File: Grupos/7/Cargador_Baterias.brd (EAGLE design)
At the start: 70.3 x 59.3 mm, 48 parts, among them M1 NUCLEO-L452RE, U1 MCP73830T-2AAI/MYY, U2 MCP73830T-2AAI/MYY, U3 MCP73830T-2AAI/MYY

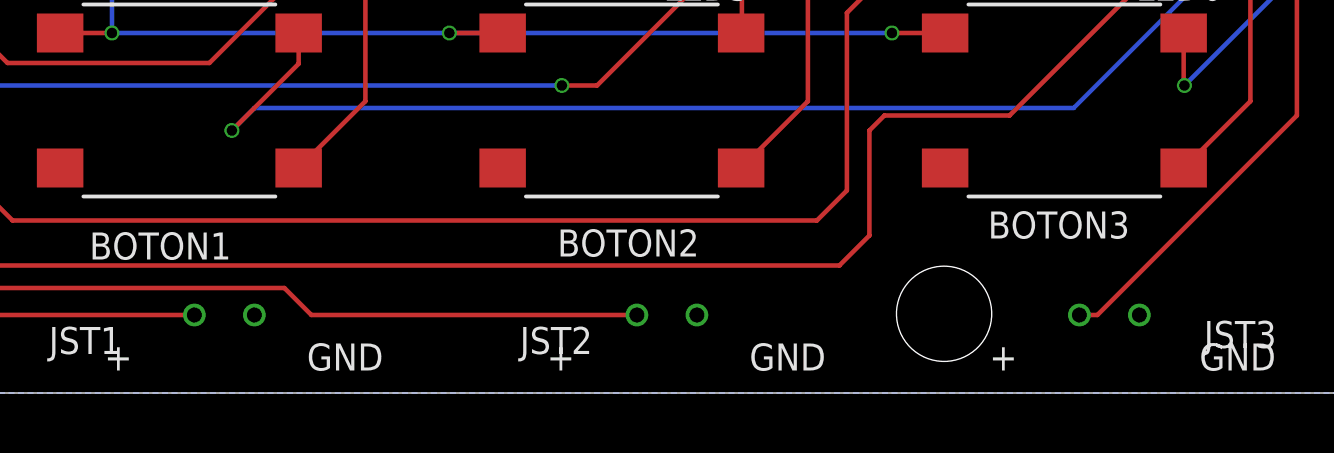
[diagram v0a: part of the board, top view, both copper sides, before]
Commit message: Se arregla JST
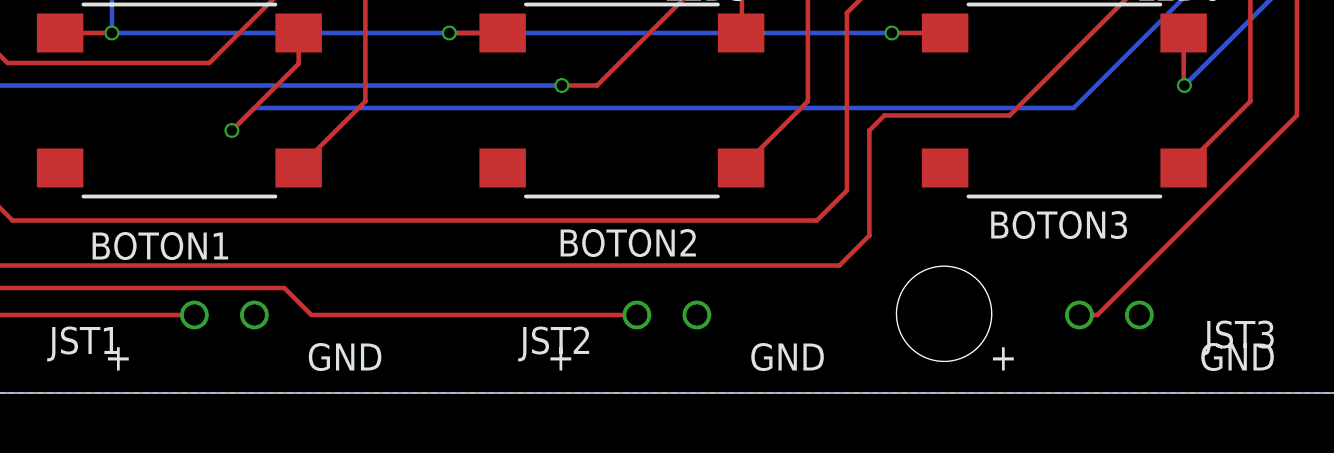
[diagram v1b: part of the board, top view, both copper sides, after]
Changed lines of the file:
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@@
 <drawing>
 <settings>
-<setting alwaysvectorfont="no"/>
+<setting alwaysvectorfont="yes"/>
 <setting verticaltext="up"/>
 </settings>
@@
 <layer number="1" name="Top" color="4" fill="1" visible="yes" active="yes"/>
 <layer number="16" name="Bottom" color="1" fill="1" visible="yes" active="yes"/>
-<layer number="17" name="Pads" color="2" fill="1" visible="no" active="yes"/>
-<layer number="18" name="Vias" color="2" fill="1" visible="no" active="yes"/>
+<layer number="17" name="Pads" color="2" fill="1" visible="yes" active="yes"/>
+<layer number="18" name="Vias" color="2" fill="1" visible="yes" active="yes"/>
 <layer number="19" name="Unrouted" color="6" fill="1" visible="no" active="yes"/>
 <layer number="20" name="Dimension" color="24" fill="1" visible="no" active="yes"/>
 <layer number="21" name="tPlace" color="7" fill="1" visible="no" active="yes"/>
 <layer number="22" name="bPlace" color="7" fill="1" visible="no" active="yes"/>
-<layer number="23" name="tOrigins" color="15" fill="1" visible="no" active="yes"/>
-<layer number="24" name="bOrigins" color="15" fill="1" visible="no" active="yes"/>
+<layer number="23" name="tOrigins" color="15" fill="1" visible="yes" active="yes"/>
+<layer number="24" name="bOrigins" color="15" fill="1" visible="yes" active="yes"/>
 <layer number="25" name="tNames" color="7" fill="1" visible="yes" active="yes"/>
 <layer number="26" name="bNames" color="7" fill="1" visible="no" active="yes"/>
@@
 <wire x1="31" y1="41.6" x2="31.0744" y2="41.5256" width="0.1524" layer="1"/>
 <wire x1="31.0744" y1="41.5256" x2="32.0256" y2="41.5256" width="0.1524" layer="1"/>
+<wire x1="59.23" y1="42.264" x2="64.31" y2="40.71500625" width="0" layer="19" extent="1-1"/>
+<wire x1="51.05" y1="39.75" x2="59.23" y2="42.264" width="0" layer="19" extent="1-1"/>
+<wire x1="43.75" y1="41.5" x2="49.5" y2="39.75" width="0" layer="19" extent="1-1"/>
+<wire x1="51.05" y1="32.25" x2="51.05" y2="39.75" width="0" layer="19" extent="1-1"/>
+<wire x1="43.75" y1="33.75" x2="49.5" y2="32.25" width="0" layer="19" extent="1-1"/>
+<wire x1="51.05" y1="24.75" x2="51.05" y2="32.25" width="0" layer="19" extent="1-1"/>
+<wire x1="52.25" y1="19.75" x2="51.05" y2="24.75" width="0" layer="19" extent="1-1"/>
+<wire x1="47.8" y1="18.3" x2="52.3" y2="18.25" width="0" layer="19" extent="1-1"/>
+<wire x1="43.3" y1="18.25" x2="47.8" y2="18.3" width="0" layer="19" extent="1-1"/>
+<wire x1="37.55" y1="18.25" x2="43.3" y2="18.25" width="0" layer="19" extent="1-1"/>
+<wire x1="33.05" y1="18.25" x2="37.55" y2="18.25" width="0" layer="19" extent="1-1"/>
+<wire x1="28.55" y1="18.25" x2="33.05" y2="18.25" width="0" layer="19" extent="1-1"/>
+<wire x1="22.8" y1="18.25" x2="28.55" y2="18.25" width="0" layer="19" extent="1-1"/>
+<wire x1="18.3" y1="18.25" x2="22.8" y2="18.25" width="0" layer="19" extent="1-1"/>
+<wire x1="13.8" y1="18.25" x2="18.3" y2="18.25" width="0" layer="19" extent="1-1"/>
+<wire x1="18.05" y1="24.75" x2="18.25" y2="19.75" width="0" layer="19" extent="1-1"/>
+<wire x1="10.97" y1="25.5" x2="16.5" y2="24.75" width="0" layer="19" extent="1-1"/>
+<wire x1="10.97" y1="28.04" x2="10.97" y2="25.5" width="0" layer="19" extent="1-1"/>
+<wire x1="5.89" y1="28.04" x2="10.97" y2="28.04" width="0" layer="19" extent="1-1"/>
+<wire x1="3.35" y1="28.04" x2="5.89" y2="28.04" width="0" layer="19" extent="1-1"/>
+<wire x1="5.89" y1="25.5" x2="5.89" y2="28.04" width="0" layer="19" extent="1-1"/>
+<wire x1="43.75" y1="26" x2="49.5" y2="24.75" width="0" layer="19" extent="1-1"/>
+<wire x1="32" y1="26.25" x2="33" y2="19.75" width="0" layer="19" extent="1-1"/>
+<wire x1="31.95" y1="30.25" x2="31" y2="27.5" width="0" layer="19" extent="1-1"/>
+<wire x1="32" y1="34" x2="31.95" y2="30.25" width="0" layer="19" extent="1-1"/>
+<wire x1="31.95" y1="38" x2="31" y2="35.25" width="0" layer="19" extent="1-1"/>
+<wire x1="32" y1="41.5" x2="31.95" y2="38" width="0" layer="19" extent="1-1"/>
+<wire x1="31.95" y1="45.75" x2="31" y2="43" width="0" layer="19" extent="1-1"/>
+<wire x1="32.5" y1="49.75" x2="31.95" y2="45.75" width="0" layer="19" extent="1-1"/>
+<wire x1="24.775" y1="54.025" x2="30.725" y2="54.025" width="0" layer="19" extent="1-1"/>
+<wire x1="20.5" y1="57.45" x2="23.425" y2="57.035" width="0" layer="19" extent="1-1"/>
+<wire x1="20.5" y1="51.3" x2="23.425" y2="53.655" width="0" layer="19" extent="1-1"/>
+<wire x1="16.5" y1="32.25" x2="10.97" y2="28.04" width="0" layer="19" extent="1-1"/>
+<wire x1="18.05" y1="39.75" x2="18.05" y2="32.25" width="0" layer="19" extent="1-1"/>
+<wire x1="5.89" y1="43.28" x2="16.5" y2="39.75" width="0" layer="19" extent="1-1"/>
+<wire x1="66.85" y1="28.01500625" x2="64.31" y2="40.71500625" width="0" layer="19" extent="1-1"/>
+<wire x1="50.5" y1="2.6" x2="52.3" y2="18.25" width="0" layer="19" extent="1-1"/>
+<wire x1="35.75" y1="2.6" x2="50.5" y2="2.6" width="0" layer="19" extent="1-1"/>
+<wire x1="21" y1="2.6" x2="35.75" y2="2.6" width="0" layer="19" extent="1-1"/>
 </signal>
 <signal name="VIN">

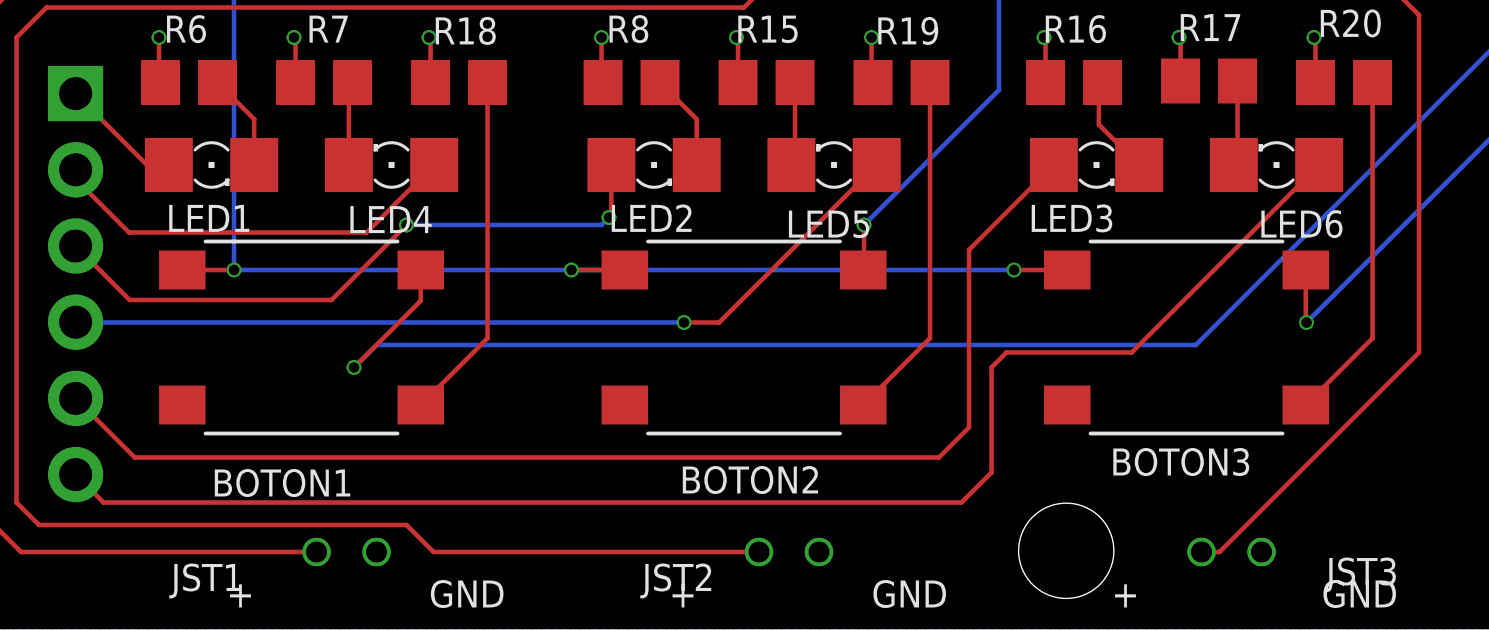
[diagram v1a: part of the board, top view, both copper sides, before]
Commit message: Se arregla botón
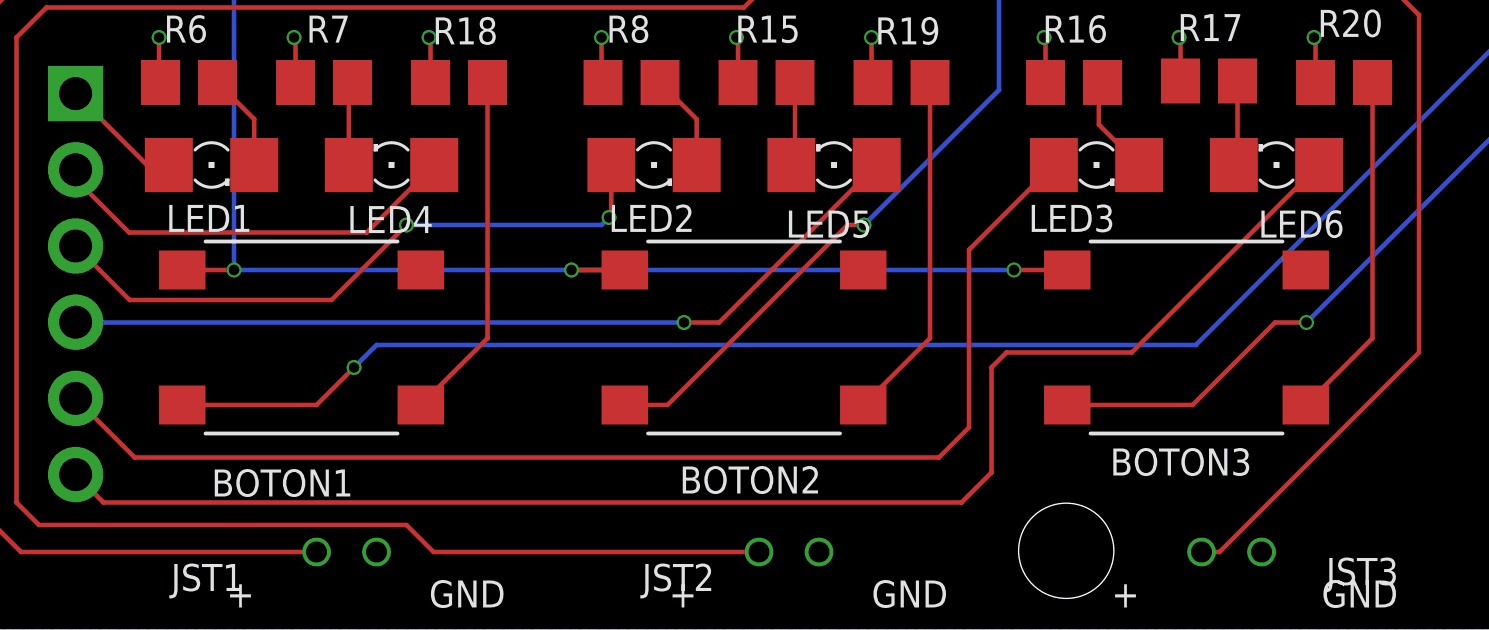
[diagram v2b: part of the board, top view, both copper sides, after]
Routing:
- net B2: track 30.2 -> 39.1 mm
- net B3: track 12.4 -> 19.8 mm
- net B1: track 48.0 -> 50.1 mm
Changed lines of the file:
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@@
 <wire x1="31" y1="41.6" x2="31.0744" y2="41.5256" width="0.1524" layer="1"/>
 <wire x1="31.0744" y1="41.5256" x2="32.0256" y2="41.5256" width="0.1524" layer="1"/>
-<wire x1="59.23" y1="42.264" x2="64.31" y2="40.71500625" width="0" layer="19" extent="1-1"/>
-<wire x1="51.05" y1="39.75" x2="59.23" y2="42.264" width="0" layer="19" extent="1-1"/>
-<wire x1="43.75" y1="41.5" x2="49.5" y2="39.75" width="0" layer="19" extent="1-1"/>
-<wire x1="51.05" y1="32.25" x2="51.05" y2="39.75" width="0" layer="19" extent="1-1"/>
-<wire x1="43.75" y1="33.75" x2="49.5" y2="32.25" width="0" layer="19" extent="1-1"/>
-<wire x1="51.05" y1="24.75" x2="51.05" y2="32.25" width="0" layer="19" extent="1-1"/>
-<wire x1="52.25" y1="19.75" x2="51.05" y2="24.75" width="0" layer="19" extent="1-1"/>
-<wire x1="47.8" y1="18.3" x2="52.3" y2="18.25" width="0" layer="19" extent="1-1"/>
-<wire x1="43.3" y1="18.25" x2="47.8" y2="18.3" width="0" layer="19" extent="1-1"/>
-<wire x1="37.55" y1="18.25" x2="43.3" y2="18.25" width="0" layer="19" extent="1-1"/>
-<wire x1="33.05" y1="18.25" x2="37.55" y2="18.25" width="0" layer="19" extent="1-1"/>
-<wire x1="28.55" y1="18.25" x2="33.05" y2="18.25" width="0" layer="19" extent="1-1"/>
-<wire x1="22.8" y1="18.25" x2="28.55" y2="18.25" width="0" layer="19" extent="1-1"/>
-<wire x1="18.3" y1="18.25" x2="22.8" y2="18.25" width="0" layer="19" extent="1-1"/>
-<wire x1="13.8" y1="18.25" x2="18.3" y2="18.25" width="0" layer="19" extent="1-1"/>
-<wire x1="18.05" y1="24.75" x2="18.25" y2="19.75" width="0" layer="19" extent="1-1"/>
-<wire x1="10.97" y1="25.5" x2="16.5" y2="24.75" width="0" layer="19" extent="1-1"/>
-<wire x1="10.97" y1="28.04" x2="10.97" y2="25.5" width="0" layer="19" extent="1-1"/>
-<wire x1="5.89" y1="28.04" x2="10.97" y2="28.04" width="0" layer="19" extent="1-1"/>
-<wire x1="3.35" y1="28.04" x2="5.89" y2="28.04" width="0" layer="19" extent="1-1"/>
-<wire x1="5.89" y1="25.5" x2="5.89" y2="28.04" width="0" layer="19" extent="1-1"/>
-<wire x1="43.75" y1="26" x2="49.5" y2="24.75" width="0" layer="19" extent="1-1"/>
-<wire x1="32" y1="26.25" x2="33" y2="19.75" width="0" layer="19" extent="1-1"/>
-<wire x1="31.95" y1="30.25" x2="31" y2="27.5" width="0" layer="19" extent="1-1"/>
-<wire x1="32" y1="34" x2="31.95" y2="30.25" width="0" layer="19" extent="1-1"/>
-<wire x1="31.95" y1="38" x2="31" y2="35.25" width="0" layer="19" extent="1-1"/>
-<wire x1="32" y1="41.5" x2="31.95" y2="38" width="0" layer="19" extent="1-1"/>
-<wire x1="31.95" y1="45.75" x2="31" y2="43" width="0" layer="19" extent="1-1"/>
-<wire x1="32.5" y1="49.75" x2="31.95" y2="45.75" width="0" layer="19" extent="1-1"/>
-<wire x1="24.775" y1="54.025" x2="30.725" y2="54.025" width="0" layer="19" extent="1-1"/>
-<wire x1="20.5" y1="57.45" x2="23.425" y2="57.035" width="0" layer="19" extent="1-1"/>
-<wire x1="20.5" y1="51.3" x2="23.425" y2="53.655" width="0" layer="19" extent="1-1"/>
-<wire x1="16.5" y1="32.25" x2="10.97" y2="28.04" width="0" layer="19" extent="1-1"/>
-<wire x1="18.05" y1="39.75" x2="18.05" y2="32.25" width="0" layer="19" extent="1-1"/>
-<wire x1="5.89" y1="43.28" x2="16.5" y2="39.75" width="0" layer="19" extent="1-1"/>
-<wire x1="66.85" y1="28.01500625" x2="64.31" y2="40.71500625" width="0" layer="19" extent="1-1"/>
-<wire x1="50.5" y1="2.6" x2="52.3" y2="18.25" width="0" layer="19" extent="1-1"/>
-<wire x1="35.75" y1="2.6" x2="50.5" y2="2.6" width="0" layer="19" extent="1-1"/>
-<wire x1="21" y1="2.6" x2="35.75" y2="2.6" width="0" layer="19" extent="1-1"/>
 </signal>
 <signal name="VIN">
@@
 </signal>
 <signal name="B1">
-<contactref element="BOTON1" pad="3"/>
 <contactref element="M1" pad="CN9-7"/>
-<wire x1="22.475" y1="12" x2="22.475" y2="10.975" width="0.1524" layer="1"/>
-<wire x1="22.475" y1="10.975" x2="20.25" y2="8.75" width="0.1524" layer="1"/>
 <via x="20.25" y="8.75" extent="1-16" drill="0.35"/>
 <wire x1="20.25" y1="8.75" x2="21" y2="9.5" width="0.1524" layer="16"/>
 <wire x1="48.31" y1="9.5" x2="59.23" y2="20.42" width="0.1524" layer="16"/>
 <wire x1="21" y1="9.5" x2="48.31" y2="9.5" width="0.1524" layer="16"/>
+<contactref element="BOTON1" pad="3"/>
+<wire x1="20.25" y1="8.75" x2="19" y2="7.5" width="0.1524" layer="1"/>
+<wire x1="19" y1="7.5" x2="14.525" y2="7.5" width="0.1524" layer="1"/>
 </signal>
 <signal name="B2">
-<contactref element="BOTON2" pad="3"/>
-<wire x1="37.225" y1="12" x2="37.25" y2="12.025" width="0.1524" layer="1"/>
-<wire x1="37.25" y1="12.025" x2="37.25" y2="13.5" width="0.1524" layer="1"/>
 <via x="37.25" y="13.5" extent="1-16" drill="0.35"/>
 <wire x1="37.25" y1="13.5" x2="41.75" y2="18" width="0.1524" layer="16"/>
@@
 <wire x1="41.96" y1="22.96" x2="59.23" y2="22.96" width="0.1524" layer="16"/>
 <wire x1="41.75" y1="18" x2="41.75" y2="22.75" width="0.1524" layer="16"/>
+<contactref element="BOTON2" pad="3"/>
+<wire x1="37.25" y1="13.5" x2="36.7" y2="13.5" width="0.1524" layer="1"/>
+<wire x1="30.7" y1="7.5" x2="29.275" y2="7.5" width="0.1524" layer="1"/>
+<wire x1="36.7" y1="13.5" x2="30.7" y2="7.5" width="0.1524" layer="1"/>
 </signal>
 <signal name="B3">
-<contactref element="BOTON3" pad="3"/>
 <contactref element="M1" pad="CN9-6"/>
-<wire x1="51.975" y1="12" x2="51.975" y2="10.275" width="0.1524" layer="1"/>
 <wire x1="51.975" y1="10.275" x2="52" y2="10.25" width="0.1524" layer="1"/>
 <via x="52" y="10.25" extent="1-16" drill="0.35"/>
 <wire x1="52" y1="10.25" x2="59.23" y2="17.48" width="0.1524" layer="16"/>
 <wire x1="59.23" y1="17.48" x2="59.23" y2="17.88" width="0.1524" layer="16"/>
+<contactref element="BOTON3" pad="3"/>
+<wire x1="44.025" y1="7.5" x2="48.2" y2="7.5" width="0.1524" layer="1"/>
+<wire x1="50.95" y1="10.25" x2="52" y2="10.25" width="0.1524" layer="1"/>
+<wire x1="48.2" y1="7.5" x2="50.95" y2="10.25" width="0.1524" layer="1"/>
 </signal>
 <signal name="N$3">
@@
 <mfgpreviewcolor name="substratecolor" color="0xFF786E46"/>
 </mfgpreviewcolors>
+<errors>
+</errors>
 </board>
 </drawing>
